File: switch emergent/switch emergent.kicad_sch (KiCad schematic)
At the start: 31 parts, among them J1 Conn_02x04_Odd_Even, J2 Conn_01x06, J3 Conn_01x09, J4 Conn_01x10, J5 Conn_01x10

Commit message: v0.2 Ordered
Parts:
- removed D3: LED, LED_SMD:LED_0603_1608Metric_Pad1.05x0.95mm_HandSolder, symbol Device:LED
- removed R7: 240, Resistor_SMD:R_0603_1608Metric_Pad0.98x0.95mm_HandSolder, symbol Device:R
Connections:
- net VBUS: no longer D5.2 (A), D6.2 (A), R1.1, R2.1
- net +3.3V: now reaches J3.3 (Pin_3), U3.30 (3V3)
- net +3.3V: now also D5.2 (A), D6.2 (A), R1.1, R2.1
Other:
- moved on the sheet: D5, D6, R10, R11

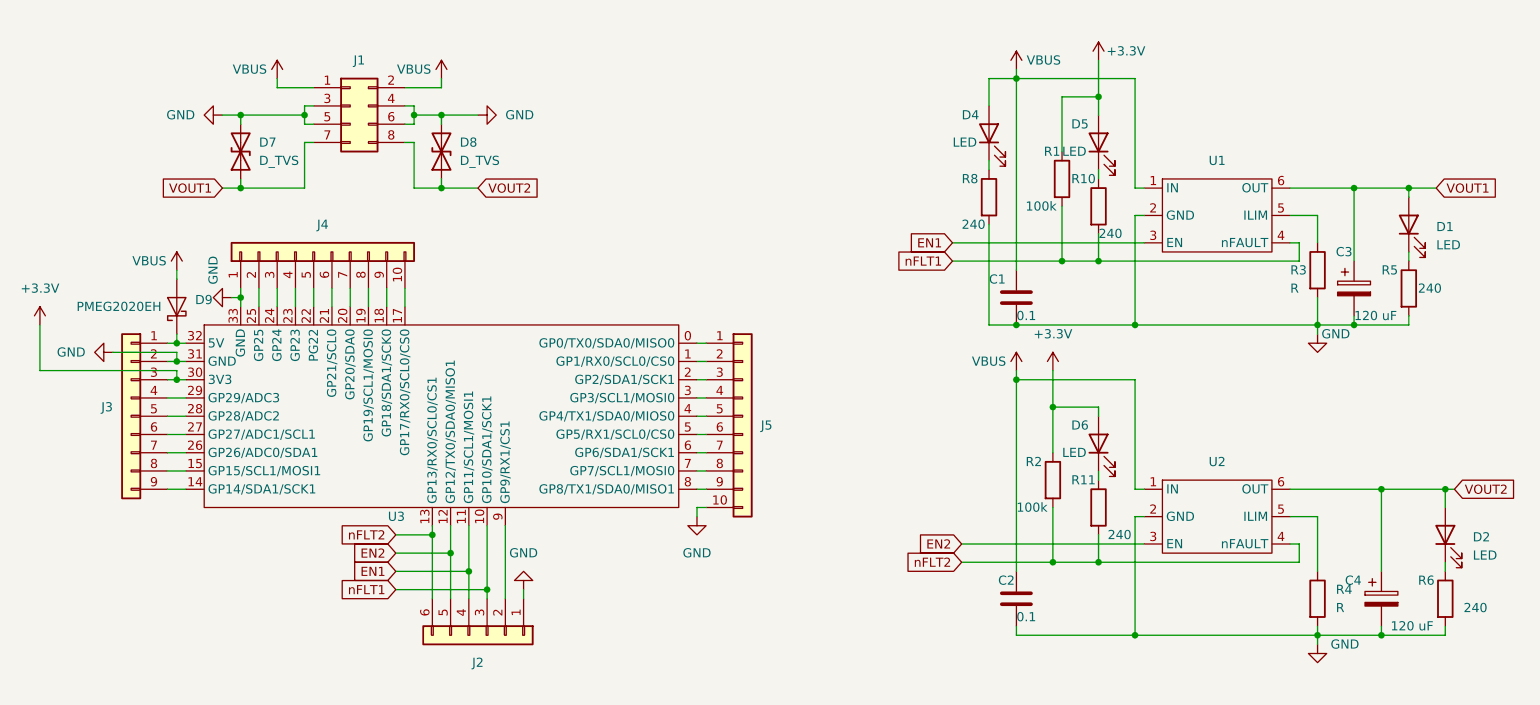
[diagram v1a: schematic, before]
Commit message: v0.3 universal PCB for embedded and remote swithces
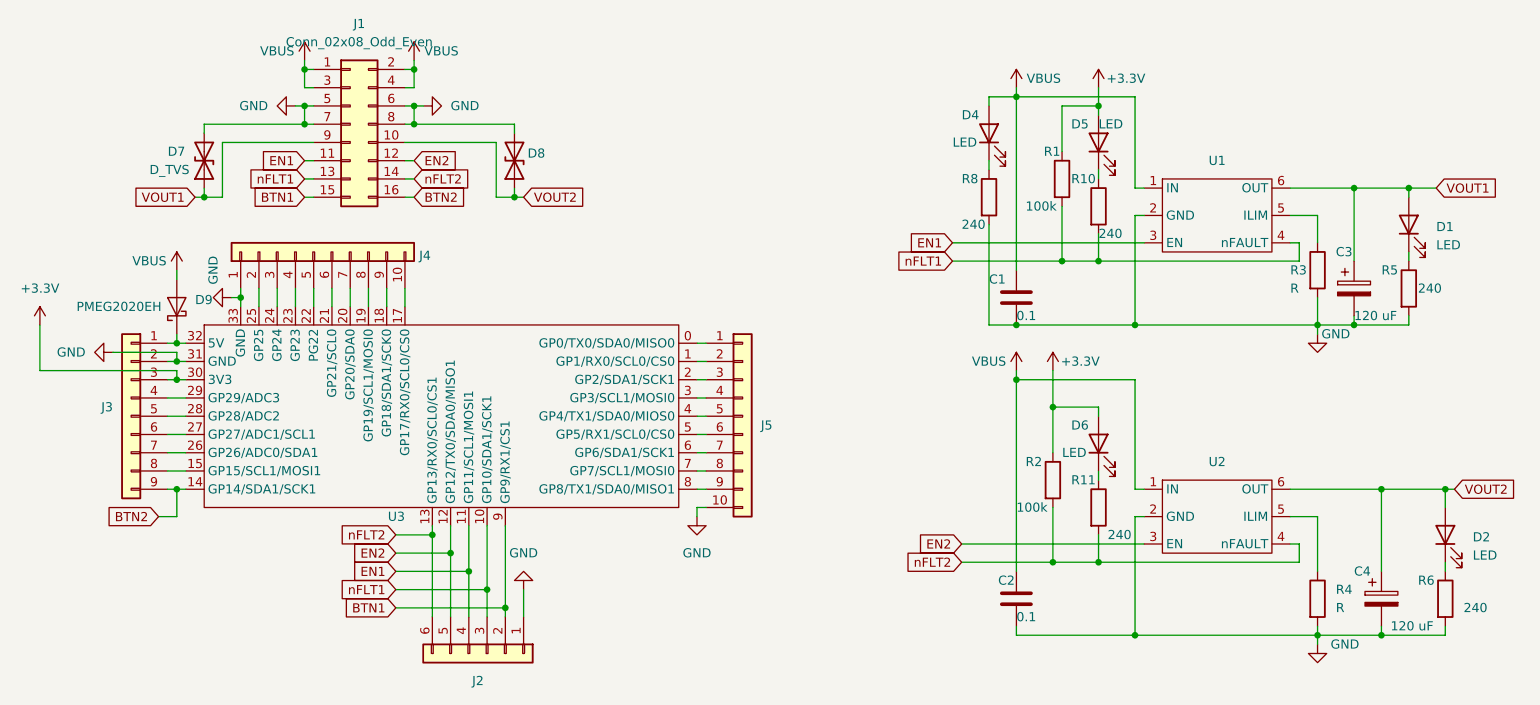
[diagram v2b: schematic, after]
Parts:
- removed J1: Conn_02x04_Odd_Even, Connector_PinSocket_2.54mm:PinSocket_2x04_P2.54mm_Vertical, symbol Connector_Generic:Conn_02x04_Odd_Even
- added J1: Conn_02x08_Odd_Even, Connector_PinSocket_2.54mm:PinSocket_2x08_P2.54mm_Vertical, symbol Connector_Generic:Conn_02x08_Odd_Even
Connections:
- net EN1: now also J1.11 (Pin_11)
- net EN2: now also J1.12 (Pin_12)
- net GND: now also J1.5 (Pin_5), J1.6 (Pin_6), J1.7 (Pin_7), J1.8 (Pin_8)
- net VBUS: now also J1.1 (Pin_1), J1.2 (Pin_2), J1.3 (Pin_3), J1.4 (Pin_4)
- net VOUT1: now also J1.9 (Pin_9)
- net VOUT2: now also J1.10 (Pin_10)
- net nFLT1: now also J1.13 (Pin_13)
- net nFLT2: now also J1.14 (Pin_14)
- net BTN2: now reaches J3.9 (Pin_9), U3.14 (GP14/SDA1/SCK1)
- net BTN2: now also J1.16 (Pin_16)
- net BTN1: now reaches J2.2 (Pin_2), U3.9 (GP9/RX1/CS1)
- net BTN1: now also J1.15 (Pin_15)
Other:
- moved on the sheet: D7, D8, J2

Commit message: v0.4 PCB uluchshaizing
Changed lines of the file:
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@@
 		(fields_autoplaced yes)
 		(property "Reference" "J1"
-			(at 60.96 11.43 0)
+			(at 60.96 13.97 0)
 			(effects
 				(font
@@
 					(size 1.27 1.27)
 				)
+				(hide yes)
 			)
 		)
